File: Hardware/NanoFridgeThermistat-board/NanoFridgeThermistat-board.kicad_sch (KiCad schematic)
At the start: 57 parts, among them J1 Connector_Thermistor, J2 Main_Connector, J3 CompressorMotor_Connector, J4 I2C_Conn, J5 Connector_Thermistor, SW1 SW_Push, SW2 SW_Push, T1 CST1, U1 MOC3042M, U2 TL072

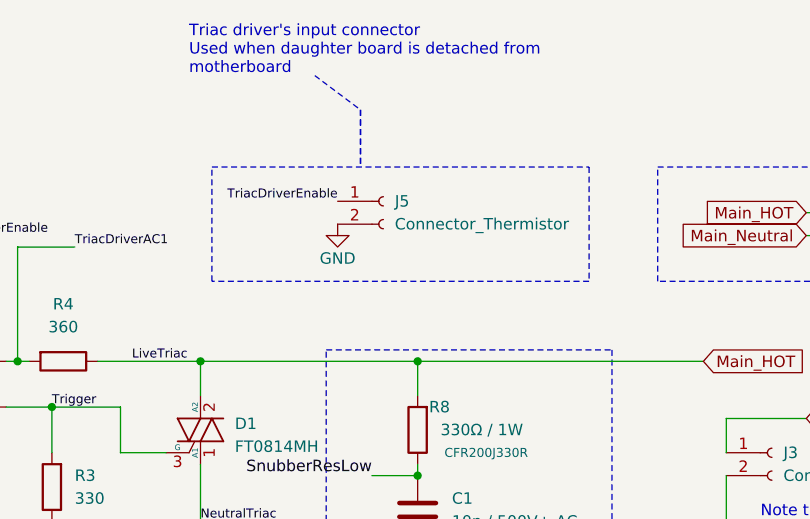
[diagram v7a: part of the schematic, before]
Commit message: Added mother-daughter boards connector on mother board as well
Signed-off-by: bebenlebricolo <benoittarrade@hotmail.fr>
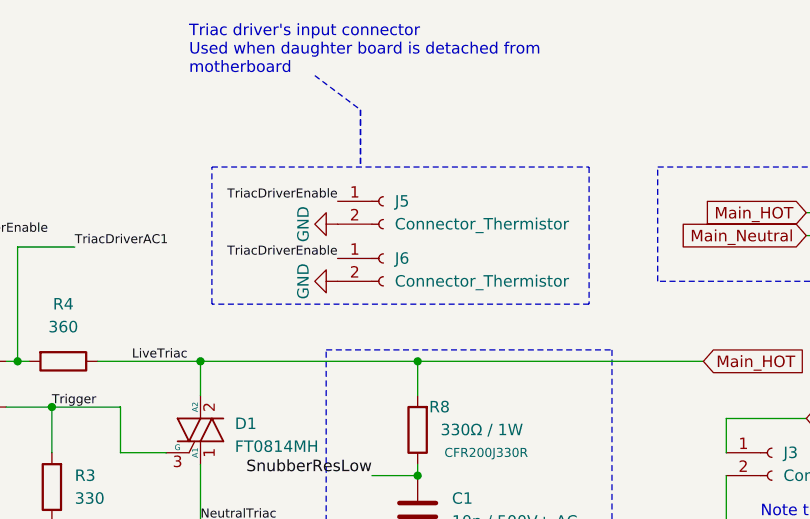
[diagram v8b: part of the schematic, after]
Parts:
- added J6: Connector_Thermistor, Connector_PinSocket_2.54mm:PinSocket_1x02_P2.54mm_Vertical, symbol Connector:Conn_01x02_Socket
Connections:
- net GND: now also J6.2 (Pin_2)
- net TriacDriverEnable: now also J6.1 (Pin_1)
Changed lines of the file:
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@@
     (fill (type none))
   )
-  (rectangle (start 158.75 13.97) (end 200.66 26.67)
+  (rectangle (start 158.75 13.97) (end 200.66 29.21)
     (stroke (width 0) (type dash_dot_dot))
     (fill (type none))
@@
     (effects (font (size 1.27 1.27)) (justify left bottom))
   )
+  (label "TriacDriverEnable" (at 172.72 24.13 180) (fields_autoplaced)
+    (effects (font (size 1 1)) (justify right bottom))
+  )
   (label "TriacDriverEnable" (at 172.72 17.78 180) (fields_autoplaced)
     (effects (font (size 1 1)) (justify right bottom))
@@
     )
   )
+  (symbol (lib_id "Connector:Conn_01x02_Socket") (at 177.8 24.13 0) (unit 1)
+    (in_bom yes) (on_board yes) (dnp no) (fields_autoplaced)
+    (property "Reference" "J6" (at 179.07 24.13 0)
+      (effects (font (size 1.27 1.27)) (justify left))
+    )
+    (property "Value" "Connector_Thermistor" (at 179.07 26.67 0)
+      (effects (font (size 1.27 1.27)) (justify left))
+    )
+    (property "Footprint" "Connector_PinSocket_2.54mm:PinSocket_1x02_P2.54mm_Vertical" (at 177.8 24.13 0)
+      (effects (font (size 1.27 1.27)) hide)
+    )
+    (property "Datasheet" "~" (at 177.8 24.13 0)
+      (effects (font (size 1.27 1.27)) hide)
+    )
+    (pin "2")
+    (pin "1")
+    (instances
+      (project "NanoFridgeThermistat-board"
+        (path "/8e662055-06e4-49d8-beed-954dc4916086"
+          (reference "J6") (unit 1)
+        )
+      )
+    )
+  )
   (symbol (lib_id "Device:R") (at 149.86 95.25 0) (unit 1)
     (in_bom yes) (on_board yes) (dnp no) (fields_autoplaced)
@@
     )
   )
-  (symbol (lib_id "power:GND") (at 172.72 20.32 0) (unit 1)
+  (symbol (lib_id "power:GND") (at 172.72 20.32 270) (unit 1)
     (in_bom yes) (on_board yes) (dnp no)
-    (property "Reference" "#PWR017" (at 172.72 26.67 0)
-      (effects (font (size 1.27 1.27)) hide)
-    )
-    (property "Value" "GND" (at 172.72 24.13 0)
+    (property "Reference" "#PWR017" (at 166.37 20.32 0)
+      (effects (font (size 1.27 1.27)) hide)
+    )
+    (property "Value" "GND" (at 168.91 20.32 0)
       (effects (font (size 1.27 1.27)))
     )
@@
         )
       )
+    )
+  )
+  (symbol (lib_id "power:GND") (at 172.72 26.67 270) (unit 1)
+    (in_bom yes) (on_board yes) (dnp no)
+    (property "Reference" "#PWR018" (at 166.37 26.67 0)
+      (effects (font (size 1.27 1.27)) hide)
+    )
+    (property "Value" "GND" (at 168.91 26.67 0)
+      (effects (font (size 1.27 1.27)))
+    )
+    (property "Footprint" "" (at 172.72 26.67 0)
+      (effects (font (size 1.27 1.27)) hide)
+    )
+    (property "Datasheet" "" (at 172.72 26.67 0)
+      (effects (font (size 1.27 1.27)) hide)
+    )
+    (pin "1")
+    (instances
+      (project "NanoFridgeThermistat-board"
+        (path "/8e662055-06e4-49d8-beed-954dc4916086"
+          (reference "#PWR018") (unit 1)
+        )
+      )
